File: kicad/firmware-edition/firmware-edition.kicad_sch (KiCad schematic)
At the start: 102 parts, among them J1 Solar Panel, J10 GPIO, J11 I2C-3V3, J12 GPIO, J13 SPI, J14 I2C-5V, J15 SWD, J16 Conn_01x03, J19 Conn_01x01_Pin, J2 BATT, J20 Conn_01x01_Pin, J21 GPIO, J22 3V3, J3 3V3 Sensor Bus, J4 Conn_01x04, J6 Conn_01x02, J8 GPIO, Q1 BSS84, Q2 BSS84, Q3 BSS84, SW1 BOOT_DFU, SW2 RST, U1 ADP5091, U2 TPS61023DRLR, U3 MAX-M10M-00B, U4 Si4463, U5 STM32U073KCU6, U6 TXS0102VDCTR, Y1 30MHz

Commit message: via stitch updates
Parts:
- SW1, SW2: footprint Button_Switch_SMD:Panasonic_EVQPUJ_EVQPUA -> Button_Switch_SMD:SW_Push_1TS009xxxx-xxxx-xxxx_6x6x5mm
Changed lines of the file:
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@@
 			)
 		)
-		(property "Footprint" "Button_Switch_SMD:Panasonic_EVQPUJ_EVQPUA"
+		(property "Footprint" "Button_Switch_SMD:SW_Push_1TS009xxxx-xxxx-xxxx_6x6x5mm"
 			(at 273.05 199.39 0)
 			(effects
@@
 			)
 		)
-		(property "Footprint" "Button_Switch_SMD:Panasonic_EVQPUJ_EVQPUA"
+		(property "Footprint" "Button_Switch_SMD:SW_Push_1TS009xxxx-xxxx-xxxx_6x6x5mm"
 			(at 299.72 196.85 0)
 			(effects

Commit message: Fixed small issues
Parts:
- J16: value Conn_01x03 -> USB_C
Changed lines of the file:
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@@
 			)
 		)
-		(property "Value" "Conn_01x03"
+		(property "Value" "USB_C"
 			(at 85.09 198.12 0)
 			(effects

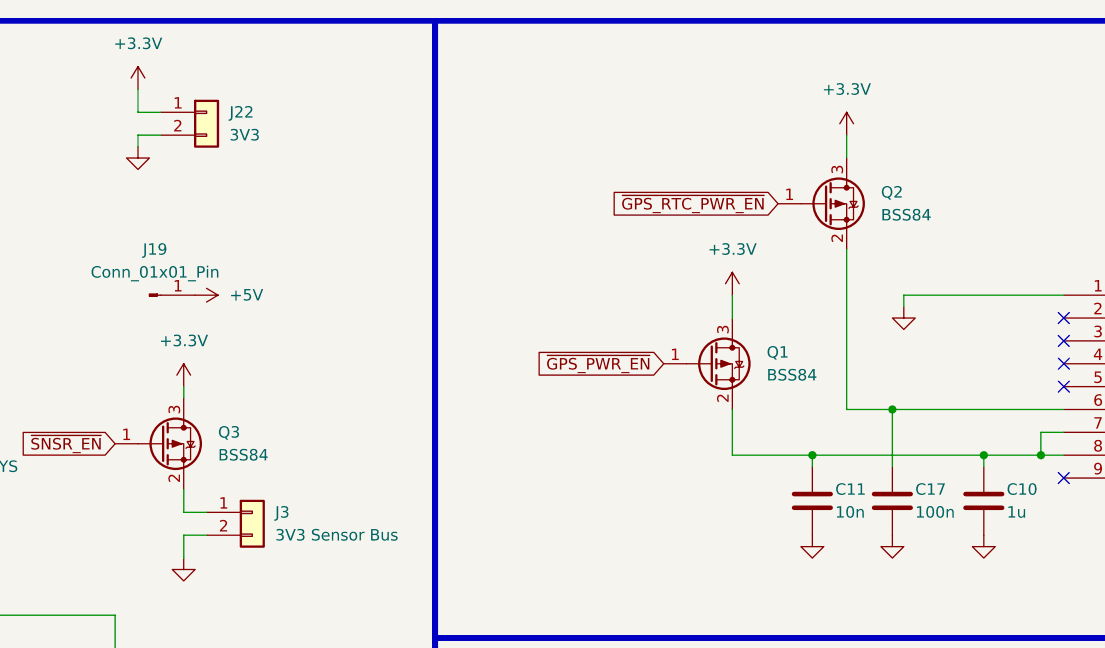
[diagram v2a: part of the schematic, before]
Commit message: transistors backwards
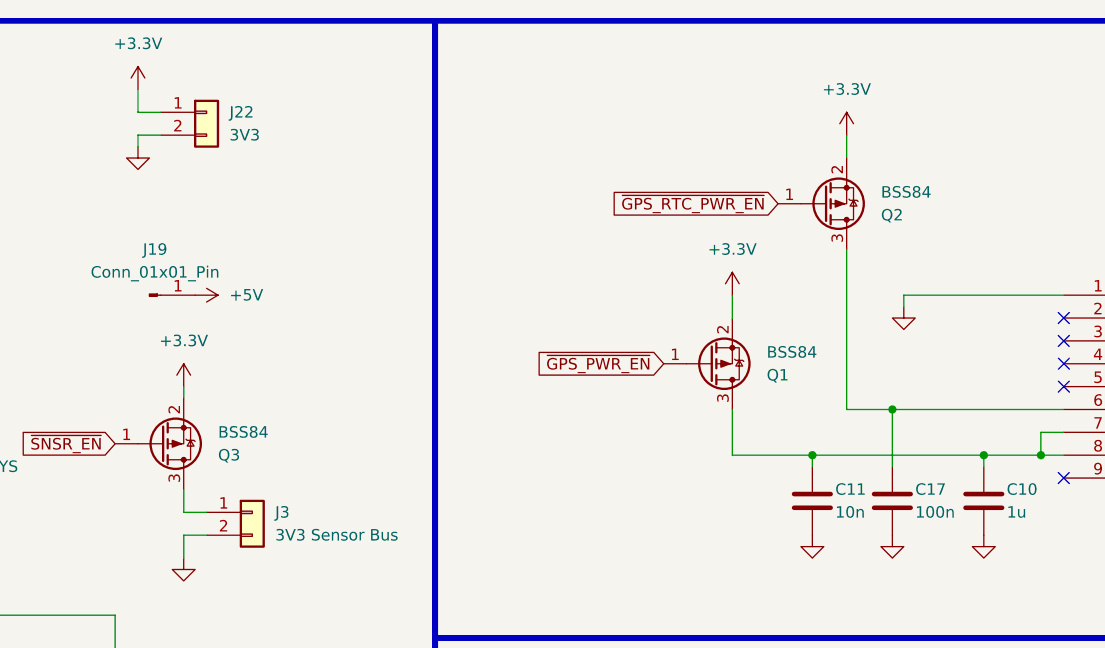
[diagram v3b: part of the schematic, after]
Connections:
- net +3.3V: now also Q1.2 (S), Q2.2 (S), Q3.2 (S); no longer Q1.3 (D), Q2.3 (D), Q3.3 (D)
- net at J3.1 (Pin_1): now also Q3.3 (D); no longer Q3.2 (S)
- net at C17.1, U3.6 (V_BCKP): now also Q2.3 (D); no longer Q2.2 (S)
- net at C10.1, C11.1, U3.7 (V_IO)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: now also Q1.3 (D); no longer Q1.2 (S)
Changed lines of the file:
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@@
 	(wire
 		(pts
-			(xy 185.42 64.77) (xy 185.42 67.31)
-		)
-		(stroke
-			(width 0)
-			(type default)
-		)
-	)
-	(wire
-		(pts
 			(xy 180.34 25.4) (xy 180.34 26.67)
 		)
@@
 	(wire
 		(pts
+			(xy 185.42 64.77) (xy 185.42 67.31)
+		)
+		(stroke
+			(width 0)
+			(type default)
+		)
+	)
+	(wire
+		(pts
 			(xy 154.94 78.74) (xy 139.7 78.74)
 		)
@@
 	(wire
 		(pts
+			(xy 185.42 53.34) (xy 185.42 54.61)
+		)
+		(stroke
+			(width 0)
+			(type default)
+		)
+	)
+	(wire
+		(pts
 			(xy 39.37 43.18) (xy 46.99 43.18)
 		)
@@
 	(wire
 		(pts
-			(xy 185.42 53.34) (xy 185.42 54.61)
-		)
-		(stroke
-			(width 0)
-			(type default)
-		)
-	)
-	(wire
-		(pts
 			(xy 280.67 58.42) (xy 280.67 60.96)
 		)
@@
 		(lib_id "Transistor_FET:BSS84")
 		(at 256.54 33.02 0)
+		(mirror x)
 		(unit 1)
 		(exclude_from_sim no)
@@
 		(on_board yes)
 		(dnp no)
-		(fields_autoplaced yes)
 		(property "Reference" "Q2"
-			(at 262.89 31.7499 0)
+			(at 262.89 34.2901 0)
 			(effects
 				(font
@@
 		)
 		(property "Value" "BSS84"
-			(at 262.89 34.2899 0)
+			(at 262.89 31.7501 0)
 			(effects
 				(font
@@
 		)
 		(property "Footprint" "Package_TO_SOT_SMD:SOT-23"
-			(at 261.62 34.925 0)
+			(at 261.62 31.115 0)
 			(effects
 				(font
@@
 		)
 		(property "Datasheet" "http://assets.nexperia.com/documents/data-sheet/BSS84.pdf"
-			(at 261.62 36.83 0)
+			(at 261.62 29.21 0)
 			(effects
 				(font
@@
 		(lib_id "Transistor_FET:BSS84")
 		(at 182.88 59.69 0)
+		(mirror x)
 		(unit 1)
 		(exclude_from_sim no)
@@
 		(on_board yes)
 		(dnp no)
-		(fields_autoplaced yes)
 		(property "Reference" "Q3"
-			(at 189.23 58.4199 0)
+			(at 189.23 60.9601 0)
 			(effects
 				(font
@@
 		)
 		(property "Value" "BSS84"
-			(at 189.23 60.9599 0)
+			(at 189.23 58.4201 0)
 			(effects
 				(font
@@
 		)
 		(property "Footprint" "Package_TO_SOT_SMD:SOT-23"
-			(at 187.96 61.595 0)
+			(at 187.96 57.785 0)
 			(effects
 				(font
@@
 		)
 		(property "Datasheet" "http://assets.nexperia.com/documents/data-sheet/BSS84.pdf"
-			(at 187.96 63.5 0)
+			(at 187.96 55.88 0)
 			(effects
 				(font
@@
 		(lib_id "Transistor_FET:BSS84")
 		(at 243.84 50.8 0)
+		(mirror x)
 		(unit 1)
 		(exclude_from_sim no)
@@
 		(on_board yes)
 		(dnp no)
-		(fields_autoplaced yes)
 		(property "Reference" "Q1"
-			(at 250.19 49.5299 0)
+			(at 250.19 52.0701 0)
 			(effects
 				(font
@@
 		)
 		(property "Value" "BSS84"
-			(at 250.19 52.0699 0)
+			(at 250.19 49.5301 0)
 			(effects
 				(font
@@
 		)
 		(property "Footprint" "Package_TO_SOT_SMD:SOT-23"
-			(at 248.92 52.705 0)
+			(at 248.92 48.895 0)
 			(effects
 				(font
@@
 		)
 		(property "Datasheet" "http://assets.nexperia.com/documents/data-sheet/BSS84.pdf"
-			(at 248.92 54.61 0)
+			(at 248.92 46.99 0)
 			(effects
 				(font

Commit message: rev1 not complete
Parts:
- removed J16: USB_C, Connector_PinHeader_2.54mm:PinHeader_1x03_P2.54mm_Vertical, symbol Connector_Generic:Conn_01x03
- removed JP1: Power Type Select, Jumper:SolderJumper-3_P1.3mm_Bridged12_Pad1.0x1.5mm, symbol Jumper:SolderJumper_3_Bridged12
- removed JP2: PTS, Jumper:SolderJumper-3_P1.3mm_Bridged12_Pad1.0x1.5mm, symbol Jumper:SolderJumper_3_Bridged12
- removed Q1, Q2, Q3: BSS84, Package_TO_SOT_SMD:SOT-23, symbol Transistor_FET:BSS84
- added J5: USB_C_Receptacle_USB2.0_16P, Connector_USB:USB_C_Receptacle_Palconn_UTC16-G, symbol Connector:USB_C_Receptacle_USB2.0_16P
- added JP1, JP3: PTS, Jumper:SolderJumper-2_P1.3mm_Open_TrianglePad1.0x1.5mm, symbol Jumper:SolderJumper_2_Open
- added Q1, Q2, Q3: GSFW0201, Package_TO_SOT_SMD:SOT-883, symbol Transistor_FET:Q_PMOS_GSD
- added R18: 0, Resistor_SMD:R_0402_1005Metric, symbol Device:R_Small
- added R19, R23: 5.1k, Resistor_SMD:R_0402_1005Metric, symbol Device:R_Small
- C1, C10, C11, C12, C13, C14, C15, C16, C17, C18, C19, C2, C20, C21, C24, C25, C26, C27, C3, C4, C5, C6, C7, C8, C9, CC1, CF2, CF3, CR1, CR2: footprint Capacitor_SMD:C_0603_1608Metric -> Capacitor_SMD:C_0402_1005Metric
- CF1: value 30p -> 13p; footprint Capacitor_SMD:C_0603_1608Metric -> Capacitor_SMD:C_0402_1005Metric
- J1: footprint Connector_PinSocket_2.54mm:PinSocket_1x02_P2.54mm_Vertical -> Connector_Wire:SolderWire-0.1sqmm_1x02_P3.6mm_D0.4mm_OD1mm; now left out of the parts list
- L3, LF2, LF3, LF4, LR2, Lchk1: footprint Inductor_SMD:L_0603_1608Metric -> Inductor_SMD:L_0402_1005Metric
- LF1: value 39n -> 91n; footprint Inductor_SMD:L_0603_1608Metric -> Inductor_SMD:L_0402_1005Metric
- LR1: value 300n -> 270n; footprint Inductor_SMD:L_0603_1608Metric -> Inductor_SMD:L_0402_1005Metric
- R1, R10, R11, R12, R13, R17, R2, R20, R21, R22, R25, R26, R3, R4, R5, R6, R7, R8, R9: footprint Resistor_SMD:R_0603_1608Metric -> Resistor_SMD:R_0402_1005Metric
- R14: value 10M -> 1M; footprint Resistor_SMD:R_0603_1608Metric -> Resistor_SMD:R_0402_1005Metric
- R15: value 1.47M -> 510k; footprint Resistor_SMD:R_0603_1608Metric -> Resistor_SMD:R_0402_1005Metric
- R16: value 200k -> 68k; footprint Resistor_SMD:R_0603_1608Metric -> Resistor_SMD:R_0402_1005Metric
- RF1: value 50 -> 51; footprint Resistor_SMD:R_0603_1608Metric -> Resistor_SMD:R_0402_1005Metric
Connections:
- net +3.3V: now also Q1.2 (S), Q2.2 (S), Q3.2 (S)
- net GND: now also J5.A1 (GND), J5.A12 (GND), J5.B1 (GND), J5.B12 (GND), R18.2, R19.2, R23.2
- net GPIO0: now also U5.15 (PB1); no longer U5.9 (PA3)
- net GPIO1: now also U5.9 (PA3); no longer U5.8 (PA2)
- net GPIO2: now also U5.8 (PA2); no longer U5.30 (PB7)
- net GPIO3: now also U5.7 (PA1); no longer U5.29 (PB6)
- net LLD: now also U5.27 (PB4); no longer U5.25 (PA15)
- net PGOOD: now also U5.29 (PB6); no longer U5.6 (PA0-CK_IN)
- net USB_D+: now also J5.A6 (D+), J5.B6 (D+)
- net USB_D-: now also J5.A7 (D-), J5.B7 (D-)
- net ~{GPS_PWR_EN}: now also U5.25 (PA15), Q1.1 (G); no longer U5.15 (PB1)
- net ~{GPS_RTC_PWR_EN}: now also U5.26 (PB3), Q2.1 (G); no longer U5.14 (PB0)
- net ~{RF_EN}: now also U5.6 (PA0-CK_IN); no longer U5.27 (PB4)
- net ~{RF_IRQ}: now also U5.14 (PB0); no longer U5.26 (PB3)
- net ~{SNSR_EN}: now also U5.30 (PB7), Q3.1 (G); no longer U5.7 (PA1)
- net at CR2.1, LR1.1: now also U4.3 (RXn); no longer U4.2 (RXp)
- net at CR1.1, LR1.2, LR2.1: now also U4.2 (RXp); no longer U4.3 (RXn)
- net at R11.1: now also JP3.1 (A)
- net at R10.1: now also R6.2, U1.4 (TERM), JP1.2 (B)
- net at R3.1, R6.1, U1.1 (REF): now also R13.1, JP3.2 (B)
- net at J3.1 (Pin_1): now also Q3.3 (D)
- net at C17.1, U3.6 (V_BCKP): now also Q2.3 (D)
- net at C10.1, C11.1, U3.7 (V_IO)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: now also Q1.3 (D)
- net at R7.1: now also JP1.1 (A)
- new net: J5.A5 (CC1), R19.1
- new net: J5.A4 (VBUS), J5.A9 (VBUS), J5.B4 (VBUS), J5.B9 (VBUS)
- new net: J5.B5 (CC2), R23.1
- new net: J5.S1 (SHIELD), R18.1
- no-connect marks 14 -> 17
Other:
- note added: "DFM - close enough 50 ohm termination"
- note added: "I2C Level Shifter 10k pullups inside"
- note added: "POWER TYPE SELECT DEFAULT = Li-Ion CLOSED = Supercap"
- moved on the sheet: CR1, CR2, LR1, LR2

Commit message: rev C(ompact) pre-review
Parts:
- removed C24: 10p, Capacitor_SMD:C_0402_1005Metric, symbol Device:C
- removed C26, C27: 0.1u, Capacitor_SMD:C_0402_1005Metric, symbol Device:C
- removed C8, C9: DNP, Capacitor_SMD:C_0402_1005Metric, symbol Device:C
- removed H1, H2, H3, H4: MountingHole, MountingHole:MountingHole_3.2mm_M3_ISO14580, symbol Mechanical:MountingHole
- removed J10, J12, J21, J8: GPIO, Connector_PinHeader_2.54mm:PinHeader_1x02_P2.54mm_Vertical, symbol Connector_Generic:Conn_01x02
- removed J11: I2C-3V3, Connector_PinHeader_2.54mm:PinHeader_1x02_P2.54mm_Vertical, symbol Connector_Generic:Conn_01x02
- removed J13: SPI, Connector_PinHeader_2.54mm:PinHeader_1x04_P2.54mm_Vertical, symbol Connector_Generic:Conn_01x04
- removed J14: I2C-5V, Connector_PinHeader_2.54mm:PinHeader_1x02_P2.54mm_Vertical, symbol Connector_Generic:Conn_01x02
- removed J19, J20: Conn_01x01_Pin, Connector_PinHeader_2.54mm:PinHeader_1x01_P2.54mm_Vertical, symbol Connector:Conn_01x01_Pin
- removed J22: 3V3, Connector_PinSocket_2.54mm:PinSocket_1x02_P2.54mm_Vertical, symbol Connector_Generic:Conn_01x02
- removed J3: 3V3 Sensor Bus, Connector_PinSocket_2.54mm:PinSocket_1x02_P2.54mm_Vertical, symbol Connector_Generic:Conn_01x02
- removed J4: Conn_01x04, Connector_PinHeader_2.54mm:PinHeader_1x04_P2.54mm_Vertical, symbol Connector_Generic:Conn_01x04
- removed J6: Conn_01x02, Connector_PinHeader_2.54mm:PinHeader_1x02_P2.54mm_Vertical, symbol Connector_Generic:Conn_01x02
- removed L2: 1u, Inductor_SMD:L_0603_1608Metric, symbol Device:L
- removed L3: 2.0n, Inductor_SMD:L_0402_1005Metric, symbol Device:L
- removed R14: 1M, Resistor_SMD:R_0402_1005Metric, symbol Device:R
- removed R15: 510k, Resistor_SMD:R_0402_1005Metric, symbol Device:R_Small
- removed R16: 68k, Resistor_SMD:R_0402_1005Metric, symbol Device:R_Small
- removed R25, R26: 0, Resistor_SMD:R_0402_1005Metric, symbol Device:R
- removed U2: TPS61023DRLR, TPS:DRL0006A, symbol TPS61023:TPS61023DRLR
- removed U6: TXS0102VDCTR, TXS0102V:SSOP8_DCT_TEX, symbol TXS0102V:TXS0102VDCTR
- removed Y1: 30MHz, Crystal:Crystal_SMD_Abracon_ABM3-2Pin_5.0x3.2mm, symbol Device:Crystal_Small
- added C22: 1u, Capacitor_SMD:C_0402_1005Metric, symbol Device:C
- added J3: Conn_01x10, Footprintsv2:CON_513389873, symbol Connector_Generic:Conn_01x10
- added U2: BME680, Package_LGA:Bosch_LGA-8_3x3mm_P0.8mm_ClockwisePinNumbering, symbol Sensor:BME680
- added Y1: 30MHz, Crystal:Crystal_SMD_2520-4Pin_2.5x2.0mm, symbol Device:Crystal_GND24_Small
- AE1: value Antenna -> Whip; footprint Footprintsv2:AC30157-01 GNSS Ceramic Chip -> Connector_Wire:SolderWirePad_1x01_SMD_1x2mm
- C12: value 2.2u -> 1u
- C3: value 0.1u -> 100n
- C6: value 10u -> 1u
- CF1: value 13p -> 33p
- CR1: value 13p -> 12p
- J1: footprint Connector_Wire:SolderWire-0.1sqmm_1x02_P3.6mm_D0.4mm_OD1mm -> Capacitor_THT:C_Disc_D3.0mm_W1.6mm_P2.50mm
- J2: footprint Connector_PinSocket_2.54mm:PinSocket_1x02_P2.54mm_Vertical -> Capacitor_THT:C_Disc_D3.0mm_W1.6mm_P2.50mm
- LF1: value 91n -> 39n
- LR2: value 150n -> 180n
- RF1: value 51 -> 49.9
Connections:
- net +5V is gone; now on net +3.3V: C6.1
- net +3.3V: now also C22.1, U2.2 (CSB), U2.6 (VDDIO), U2.8 (VDD)
- net GND: now also C22.2, J3.1 (Pin_1), U2.1 (GND), U2.5 (SDO), U2.7 (GND), Y1.2, Y1.4
- net MISO: now also J3.4 (Pin_4)
- net MOSI: now also J3.5 (Pin_5)
- net SCLK: now also J3.3 (Pin_3)
- net RXN: now reaches CR2.1, LR1.1, U4.3 (RXn)
- net RXP: now reaches CR1.1, LR1.2, LR2.1, U4.2 (RXp)
- net at AE1.1 (A): now also U3.11 (RF_IN)
- net at U4.17 (XIN): now also Y1.1
- net at U4.16 (XOUT): now also Y1.3
- net 3V3_SNSR: now reaches Q3.3 (D)
- net 3V3_SNSR: now also J3.2 (Pin_2)
- net 5V_EN renamed SNSR_FLEX1
- net SNSR_FLEX1: now also J3.6 (Pin_6)
- net GPIO2: no longer names the net of U4.19 (GPIO2)
- net GPIO2: no longer U5.8 (PA2)
- net GPIO3: no longer names the net of U4.20 (GPIO3)
- net GPIO3: no longer U5.7 (PA1)
- net GPS_SCL renamed SCL
- net SCL: now also J3.7 (Pin_7), U2.4 (SCK)
- net GPS_SDA renamed SDA
- net SDA: now also J3.8 (Pin_8), U2.3 (SDI)
- new net SNSR_FLEX2: J3.9 (Pin_9), U5.7 (PA1)
- new net SNSR_FLEX3: J3.10 (Pin_10), U5.8 (PA2)
- no-connect marks 17 -> 19
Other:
- note added: "BME680"
- note added: "BME688 pin-compatible"
- note added: "Power"
- note added: "any PMOS 3V3 gate"
- note removed: "I2C Level Shifter 10k pullups inside"
- note removed: "Power Subsystem"
- note removed: "pulldown draws quiescent but necessary to avoid potential MCU frying"
- moved on the sheet: AE1, C1, C18, C19, C2, C20, C21, C3, C4, C5, C7, D1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
